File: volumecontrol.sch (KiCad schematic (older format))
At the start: 46 parts, among them J4 AudioJack2, J5 AudioJack2, Q7 2N3904, U4 TL074, U5 TL072

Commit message: completely connected
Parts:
- removed C38: 100n, Capacitor_THT:C_Rect_L7.2mm_W2.5mm_P5.00mm_FKS2_FKP2_MKS2_MKP2, symbol Device:C
- removed D6: LED, LED_THT:LED_D3.0mm, symbol Device:LED
- removed J5: AudioJack2, Eurorack:PJ302M, symbol Connector:AudioJack2
- removed R40: 100k, Resistor_THT:R_Axial_DIN0204_L3.6mm_D1.6mm_P7.62mm_Horizontal, symbol Device:R
- removed R42: 47k, Resistor_THT:R_Axial_DIN0204_L3.6mm_D1.6mm_P7.62mm_Horizontal, symbol Device:R
- removed R48: 220k, Resistor_THT:R_Axial_DIN0204_L3.6mm_D1.6mm_P7.62mm_Horizontal, symbol Device:R
- removed R50: 1M, Resistor_THT:R_Axial_DIN0204_L3.6mm_D1.6mm_P7.62mm_Horizontal, symbol Device:R
- removed R51, R52, R53: 10k, Resistor_THT:R_Axial_DIN0204_L3.6mm_D1.6mm_P7.62mm_Horizontal, symbol Device:R
- removed R55: 1k, Resistor_THT:R_Axial_DIN0204_L3.6mm_D1.6mm_P7.62mm_Horizontal, symbol Device:R
- removed RV6: 100k, Potentiometer_THT:Potentiometer_Alps_RK163_Single_Horizontal, symbol Device:R_POT
- removed unit 2 of U5
- added C39, C40, C42, C43: 100n, Capacitor_THT:C_Rect_L7.2mm_W2.5mm_P5.00mm_FKS2_FKP2_MKS2_MKP2, symbol Device:C
- added RV7: 100k, Potentiometer_THT:Potentiometer_Alps_RK163_Single_Horizontal, symbol Device:R_POT
- added unit 4 of U5
- C31: renamed from C29; footprint Capacitor_THT:C_Rect_L7.0mm_W6.5mm_P5.00mm -> Eurorack:Variable_Capacitor_W6.5mm_P5.00mm
- C32: renamed from C30; value 22p -> 47p
- C38: renamed from C36; value 33n -> 100n
- R44: renamed from R45; value 100k -> 220k
- R47: renamed from R43; value 100k -> 5k
- R48: renamed from R44; value 100k -> 10k
- RV5: renamed from RV4; footprint Potentiometer_THT:Potentiometer_Alps_RK163_Single_Horizontal -> Potentiometer_THT:Potentiometer_Bourns_3296W_Vertical
- U2: renamed from U5; value TL072 -> TL074; footprint Package_DIP:DIP-8_W7.62mm_LongPads -> Package_DIP:DIP-14_W7.62mm_LongPads; symbol Amplifier_Operational:TL072 -> Amplifier_Operational:TL074
- renumbered C31 to C33, C32 to C34, C33 to C35, C34 to C36, C35 to C37, C37 to C41, D4 to D5, D5 to D6, R35 to R38, R36 to R39, R37 to R40, R38 to R41, R39 to R42, R41 to R43, R46 to R45, R47 to R46, R54 to R49, R49 to R50, RV5 to RV6, U4 to U2, U4 to U5
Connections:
- net +12V: now also RV5.3, U2.4 (V+), C39.1, C42.1, RV7.3; no longer RV5.1, U2.8 (V+)
- net -12V: now also RV5.1, U2.11 (V-), C40.1, C43.1, RV7.1; no longer U2.4 (V-)
- net GND: now also C39.2, C40.2, C42.2, C43.2; no longer RV5.3
- net VolumeControlOut: now also U5.13 (-), U5.14; no longer J4.T, R50.1
- net at R48.1: now also R47.1, U5.9 (-); no longer U5.2 (-)
- net at RV5.2: now also R43.1, U5.3 (+)
- net at R44.2, U5.1: now also U5.2 (-); no longer R48.2
- net at C41.1, U5.10 (+): now also R46.1, RV7.2
- new net: J4.T, R50.1
- new net: R50.2, U2.6 (-), U2.7
- new net: R48.2, U2.3 (+), U2.5 (+), U5.12 (+), U5.8
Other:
- note added: "Noise Reduction Filter\nPre and post amp"
- note added: "VC1 Double Led"
- note added: "Zero Point Adjust / Buffer"
- note removed: "Gate Led"
- note removed: "Gate Out"
- note removed: "Noise Reduction Filter"
- note removed: "TODO: BUFFER"
- note removed: "VC Double Led"
- note removed: "Zero Point Adjust"
- moved on the sheet: AE2, C31, C32, C33, C34, C35, C36, C37, C41, D5, D6, J4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

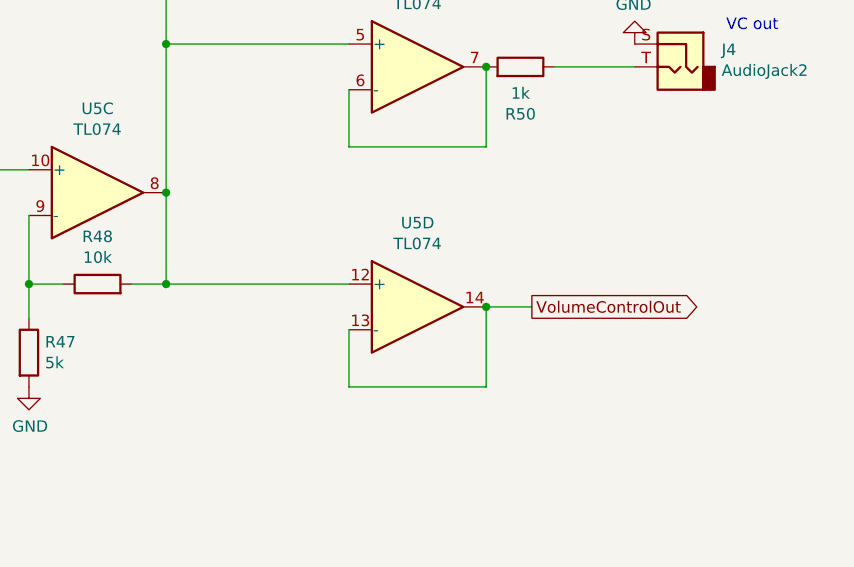
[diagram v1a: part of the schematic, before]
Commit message: add phones output
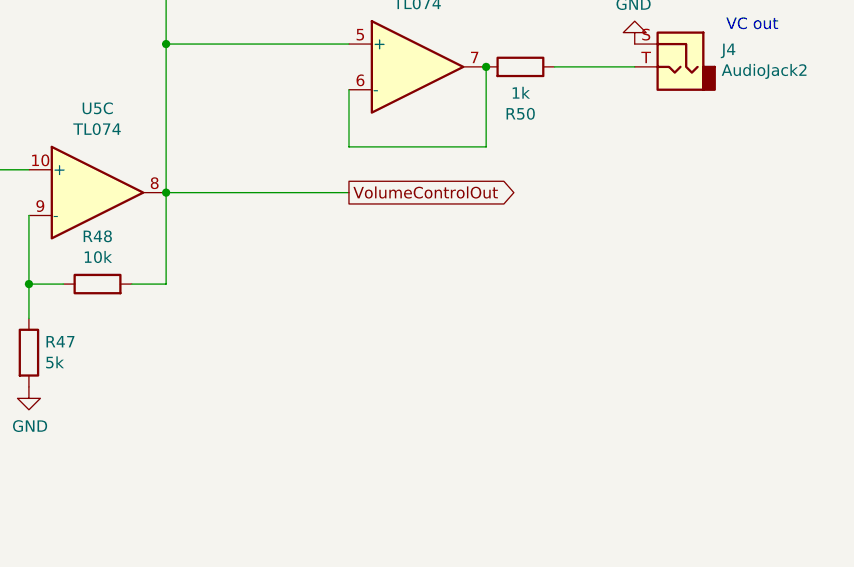
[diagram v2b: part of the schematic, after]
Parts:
- removed unit 4 of U5
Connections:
- net VolumeControlOut: now also R48.2, U2.3 (+), U2.5 (+), U5.8
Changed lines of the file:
@@
 	2050 2150 2050 1650
 Connection ~ 2050 1650
-Text GLabel 9750 2900 2    50   Output ~ 0
+Text GLabel 8950 2400 2    50   Output ~ 0
 VolumeControlOut
 Wire Wire Line
@@
 Connection ~ 7300 5300
 Wire Wire Line
-	8950 2800 8150 2800
-Connection ~ 8150 2800
+	8950 2400 8150 2400
 Connection ~ 8150 1750
 Wire Wire Line
@@
 Wire Wire Line
 	8950 900  8150 900
-Wire Wire Line
-	9550 2900 9750 2900
-Wire Wire Line
-	8950 3250 8950 3000
-Wire Wire Line
-	8950 3250 9550 3250
-Wire Wire Line
-	9550 3250 9550 2900
-Connection ~ 9550 2900
 $Comp
 L Amplifier_Operational:TL074 U2
@@
 	1    0    0    -1
 $EndComp
-$Comp
-L Amplifier_Operational:TL074 U5
-U 4 1 5F7B59C8
-P 9250 2900
-F 0 "U5" H 9250 3267 50  0000 C CNN
-F 1 "TL074" H 9250 3176 50  0000 C CNN
-F 2 "Package_DIP:DIP-14_W7.62mm_LongPads" H 9200 3000 50  0001 C CNN
-F 3 "http://www.ti.com/lit/ds/symlink/tl071.pdf" H 9300 3100 50  0001 C CNN
-	4    9250 2900
-	1    0    0    -1
-$EndComp

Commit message: removed 2 opamp units
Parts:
- removed C42, C43: 100n, Capacitor_THT:C_Rect_L7.2mm_W2.5mm_P5.00mm_FKS2_FKP2_MKS2_MKP2, symbol Device:C
- removed R43: 100k, Resistor_THT:R_Axial_DIN0204_L3.6mm_D1.6mm_P7.62mm_Horizontal, symbol Device:R
- removed RV7: 100k, Potentiometer_THT:Potentiometer_Alps_RK163_Single_Horizontal, symbol Device:R_POT
- removed unit 1 of U5
- added R45: 220k, Resistor_THT:R_Axial_DIN0204_L3.6mm_D1.6mm_P7.62mm_Horizontal, symbol Device:R
- added R51, R52: 10k, Resistor_THT:R_Axial_DIN0204_L3.6mm_D1.6mm_P7.62mm_Horizontal, symbol Device:R
- added TP4, TP5: TestPoint, TestPoint:TestPoint_THTPad_1.0x1.0mm_Drill0.5mm, symbol Connector:TestPoint
- D4: renamed from D6; symbol Device:LED_Dual_2pin -> Device:LED
- R49: renamed from R47; value 5k -> 10k
- RV9: renamed from RV6; footprint Potentiometer_THT:Potentiometer_Alps_RK163_Single_Horizontal -> Potentiometer_THT:Potentiometer_Vishay_T73YP_Vertical
- U3: renamed from U2; value TL074 -> TL072; footprint Package_DIP:DIP-14_W7.62mm_LongPads -> Package_DIP:DIP-8_W7.62mm_LongPads; symbol Amplifier_Operational:TL074 -> Amplifier_Operational:TL072
- renumbered C31 to C27, C32 to C28, C33 to C29, C34 to C30, C35 to C31, C36 to C32, C37 to C33, C38 to C34, C39 to C35, C40 to C36, C41 to C37, D5 to D3, R38 to R40, R39 to R41, R40 to R42, R41 to R43, R42 to R44, R44 to R46, R45 to R47, R46 to R48, R48 to R50, R49 to R54, R50 to R55, RV5 to RV8, U5 to U2
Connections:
- net +12V: now also U3.8 (V+); no longer U3.4 (V+)
- net -12V: now also U3.4 (V-); no longer U3.11 (V-)
- net GND: now also D4.1 (K), U2.3 (+); no longer D4.2 (AK)
- net VolumeControlOut: now also R51.2; no longer U2.5 (+), U3.3 (+)
- net at RV8.2: now also R45.2
- net at C33.2, D3.1 (K): now also R46.2
- net at C34.1, R46.1, U2.5 (+): now also R45.1
- net at C37.1, R48.1, U2.10 (+): now also TP5.1
- net at R54.1: now also D4.2 (A); no longer D4.1 (KA)
- net at C33.1, L8.2, Q7.1 (E)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: now also TP4.1
- new net: R52.2, R55.2, U2.1, U3.3 (+)
- new net: R51.1, R52.1, U2.2 (-)
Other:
- note added: "CV1 out"
- note added: "VC1 Led"
- note added: "Zero Point Adjust:\nset max to zero"
- note removed: "VC out"
- note removed: "VC1 Double Led"
- note removed: "Zero Point Adjust / Buffer"
- moved on the sheet: C34, C37, J4, R46, R47, R48, R49, R50, R54, R55, RV8, RV9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

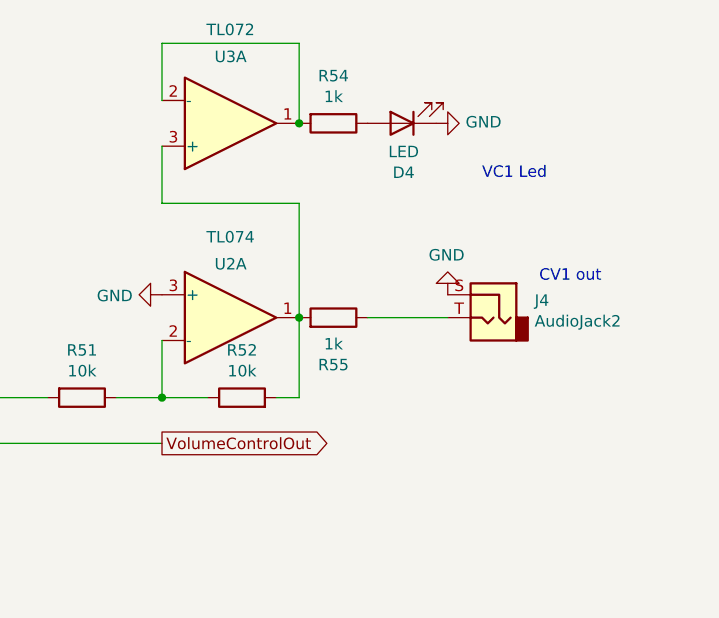
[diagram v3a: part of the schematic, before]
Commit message: full connection before relayouting labels
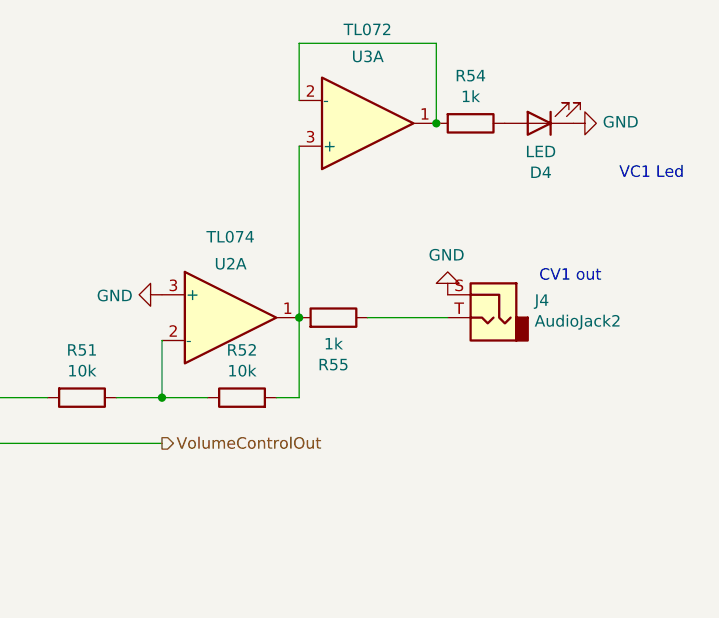
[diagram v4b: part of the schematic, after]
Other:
- moved on the sheet: D4, R54, U3A
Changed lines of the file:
@@
 $Descr A4 11693 8268
 encoding utf-8
-Sheet 2 3
+Sheet 2 4
 Title ""
 Date ""
@@
 L Device:LED D4
 U 1 1 5E6EC66A
-P 9150 1100
-F 0 "D4" H 9143 1316 50  0000 C CNN
-F 1 "LED" H 9143 1225 50  0000 C CNN
-F 2 "LED_THT:LED_D3.0mm" H 9150 1100 50  0001 C CNN
-F 3 "~" H 9150 1100 50  0001 C CNN
-	1    9150 1100
+P 9750 1100
+F 0 "D4" H 9743 1316 50  0000 C CNN
+F 1 "LED" H 9743 1225 50  0000 C CNN
+F 2 "LED_THT:LED_D3.0mm" H 9750 1100 50  0001 C CNN
+F 3 "~" H 9750 1100 50  0001 C CNN
+	1    9750 1100
 	-1   0    0    1
 $EndComp
@@
 L power:GND #PWR056
 U 1 1 5E6F56A0
-P 9300 1100
-F 0 "#PWR056" H 9300 850 50  0001 C CNN
-F 1 "GND" V 9305 972 50  0000 R CNN
-F 2 "" H 9300 1100 50  0001 C CNN
-F 3 "" H 9300 1100 50  0001 C CNN
-	1    9300 1100
+P 9900 1100
+F 0 "#PWR056" H 9900 850 50  0001 C CNN
+F 1 "GND" V 9905 972 50  0000 R CNN
+F 2 "" H 9900 1100 50  0001 C CNN
+F 3 "" H 9900 1100 50  0001 C CNN
+	1    9900 1100
 	0    -1   -1   0
 $EndComp
@@
 L Device:R R54
 U 1 1 5E72F23D
-P 8850 1100
-F 0 "R54" V 8643 1100 50  0000 C CNN
-F 1 "1k" V 8734 1100 50  0000 C CNN
-F 2 "Resistor_THT:R_Axial_DIN0204_L3.6mm_D1.6mm_P7.62mm_Horizontal" V 8780 1100 50  0001 C CNN
-F 3 "~" H 8850 1100 50  0001 C CNN
-	1    8850 1100
+P 9450 1100
+F 0 "R54" V 9243 1100 50  0000 C CNN
+F 1 "1k" V 9334 1100 50  0000 C CNN
+F 2 "Resistor_THT:R_Axial_DIN0204_L3.6mm_D1.6mm_P7.62mm_Horizontal" V 9380 1100 50  0001 C CNN
+F 3 "~" H 9450 1100 50  0001 C CNN
+	1    9450 1100
 	0    1    1    0
 $EndComp
@@
 	2050 2150 2050 1650
 Connection ~ 2050 1650
-Text GLabel 8100 2500 2    50   Output ~ 0
-VolumeControlOut
 Wire Wire Line
 	9350 1950 9000 1950
@@
 Text Notes 5250 3250 0    50   ~ 0
 Noise Reduction Filter\nPre and post amp
-Text Notes 9500 1350 0    50   ~ 0
+Text Notes 10100 1350 0    50   ~ 0
 VC1 Led
 Text Notes 9750 1800 0    50   ~ 0
@@
 L Amplifier_Operational:TL072 U3
 U 1 1 5E7B51FF
-P 8400 1100
-F 0 "U3" H 8400 809 50  0000 C CNN
-F 1 "TL072" H 8400 691 50  0000 C CNN
-F 2 "Package_DIP:DIP-8_W7.62mm_LongPads" H 8350 1200 50  0001 C CNN
-F 3 "http://www.ti.com/lit/ds/symlink/tl071.pdf" H 8450 1300 50  0001 C CNN
-	1    8400 1100
+P 9000 1100
+F 0 "U3" H 9000 809 50  0000 C CNN
+F 1 "TL072" H 9000 691 50  0000 C CNN
+F 2 "Package_DIP:DIP-8_W7.62mm_LongPads" H 8950 1200 50  0001 C CNN
+F 3 "http://www.ti.com/lit/ds/symlink/tl071.pdf" H 9050 1300 50  0001 C CNN
+	1    9000 1100
 	1    0    0    1
 $EndComp
@@
 $EndComp
 Wire Wire Line
-	8700 1950 8700 1450
-Wire Wire Line
-	8700 1450 8100 1450
-Wire Wire Line
-	8100 1450 8100 1200
-Wire Wire Line
-	8100 1000 8100 750
-Wire Wire Line
-	8100 750  8700 750
-Wire Wire Line
-	8700 750  8700 1100
-Connection ~ 8700 1100
+	8700 1000 8700 750
+Wire Wire Line
+	8700 750  9300 750
+Wire Wire Line
+	9300 750  9300 1100
+Connection ~ 9300 1100
 $Comp
 L Device:L L8
@@
 Wire Wire Line
 	6100 2400 6100 2100
+Text HLabel 8100 2500 2    50   Output ~ 0
+VolumeControlOut
+Wire Wire Line
+	8700 1200 8700 1950
 $EndSCHEMATC

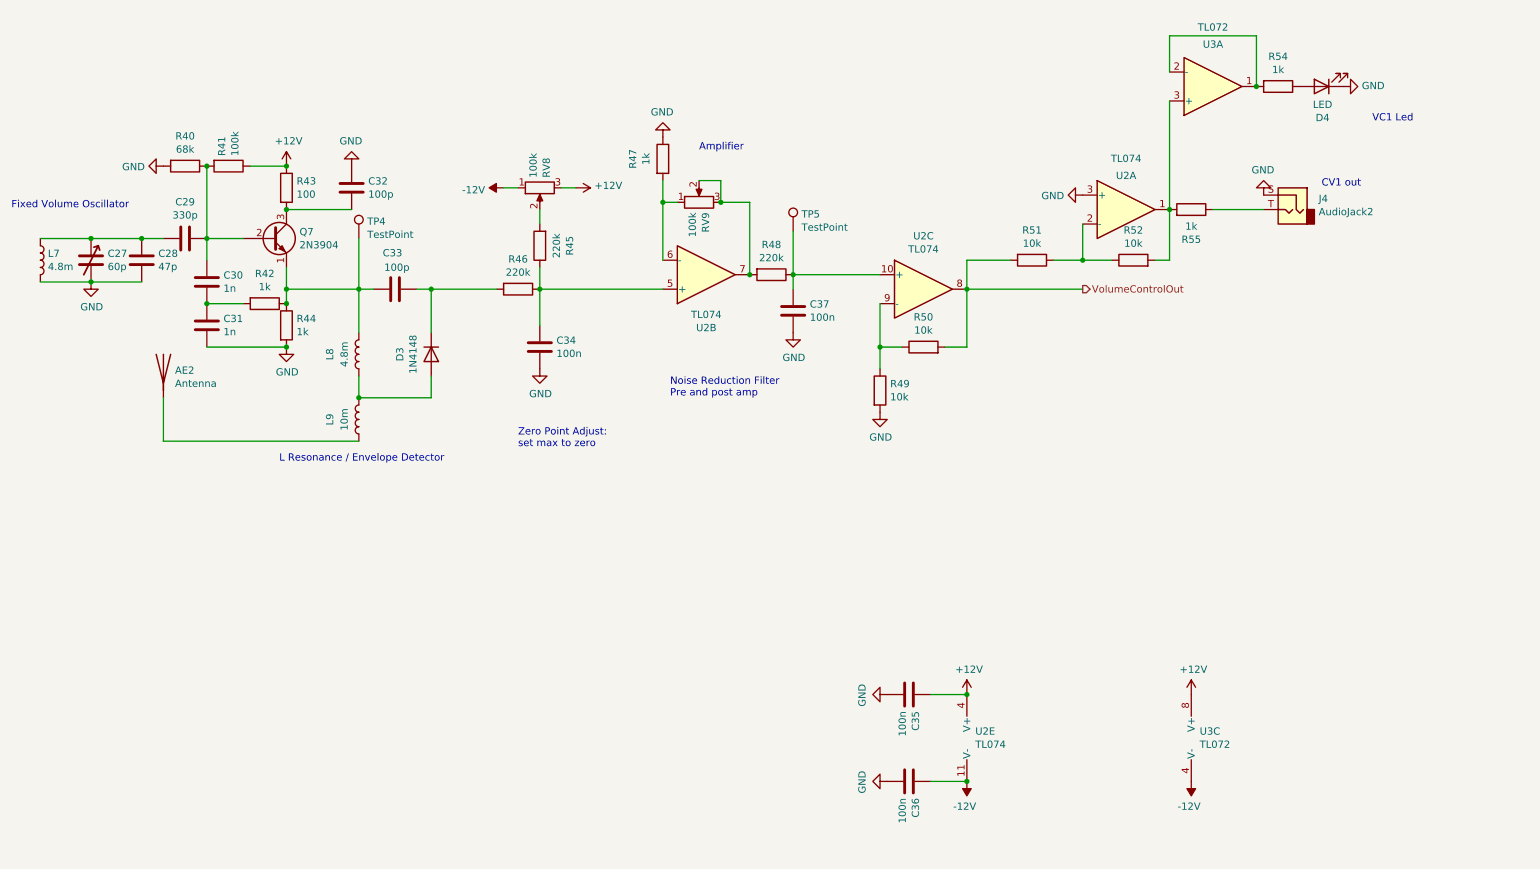
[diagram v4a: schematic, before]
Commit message: migrate audio processing to new sheet
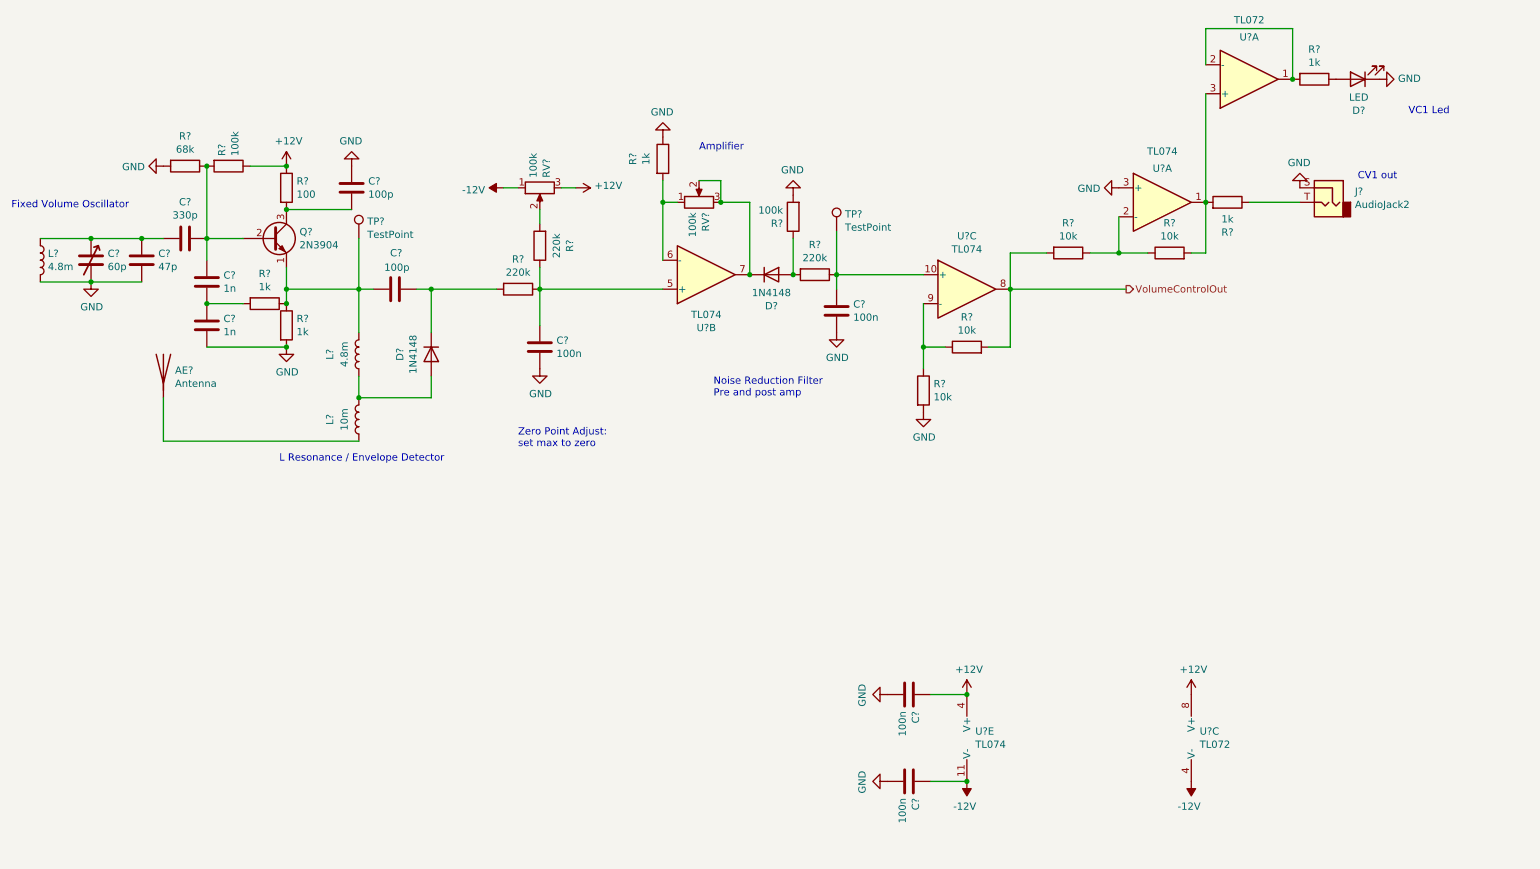
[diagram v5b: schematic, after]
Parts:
- added D8: 1N4148, Diode_THT:D_DO-34_SOD68_P7.62mm_Horizontal, symbol Device:D
- added R19: 100k, Resistor_THT:R_Axial_DIN0204_L3.6mm_D1.6mm_P7.62mm_Horizontal, symbol Device:R
- D3: footprint Diode_THT:D_DO-35_SOD27_P7.62mm_Horizontal -> Diode_THT:D_DO-34_SOD68_P7.62mm_Horizontal
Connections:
- net GND: now also R19.2
- net at RV9.2, RV9.3, U2.7: now also D8.1 (K); no longer R48.2
- new net: D8.2 (A), R19.1, R48.2
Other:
- moved on the sheet: C?, D?, J?, R?, TP?, U?A, U?C

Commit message: 1.0 for fabrication
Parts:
- R43: renamed from R45; value 220k -> 330k
- RV9: footprint Potentiometer_THT:Potentiometer_Vishay_T73YP_Vertical -> Potentiometer_THT:Potentiometer_Bourns_3386P_Vertical
- renumbered C27 to C18, C28 to C27, C29 to C28, C30 to C29, C31 to C30, C32 to C31, C33 to C32, C34 to C33, C37 to C34, D8 to D4, D4 to D8, R40 to R19, R41 to R24, R42 to R29, R43 to R40, R44 to R41, R46 to R42, R47 to R44, R19 to R45, R48 to R46, R49 to R47, R50 to R48, R51 to R49, R52 to R50, R55 to R51, R54 to R52

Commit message: add panels
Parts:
- C31: value 100p -> 100n
- L8: value 4.8m -> 1m
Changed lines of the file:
@@
 P 3050 1800
 F 0 "C31" H 3165 1846 50  0000 L CNN
-F 1 "100p" H 3165 1755 50  0000 L CNN
+F 1 "100n" H 3165 1755 50  0000 L CNN
 F 2 "Capacitor_THT:C_Rect_L7.2mm_W2.5mm_P5.00mm_FKS2_FKP2_MKS2_MKP2" H 3088 1650 50  0001 C CNN
 F 3 "~" H 3050 1800 50  0001 C CNN
@@
 P 3100 2950
 F 0 "L8" V 3300 2950 50  0000 C CNN
-F 1 "4.8m" V 3200 2950 50  0000 C CNN
+F 1 "1m" V 3200 2950 50  0000 C CNN
 F 2 "Inductor_THT:L_Axial_L12.0mm_D5.0mm_P15.24mm_Horizontal_Fastron_MISC" H 3100 2950 50  0001 C CNN
 F 3 "~" H 3100 2950 50  0001 C CNN
